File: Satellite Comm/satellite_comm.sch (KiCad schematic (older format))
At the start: 4 parts

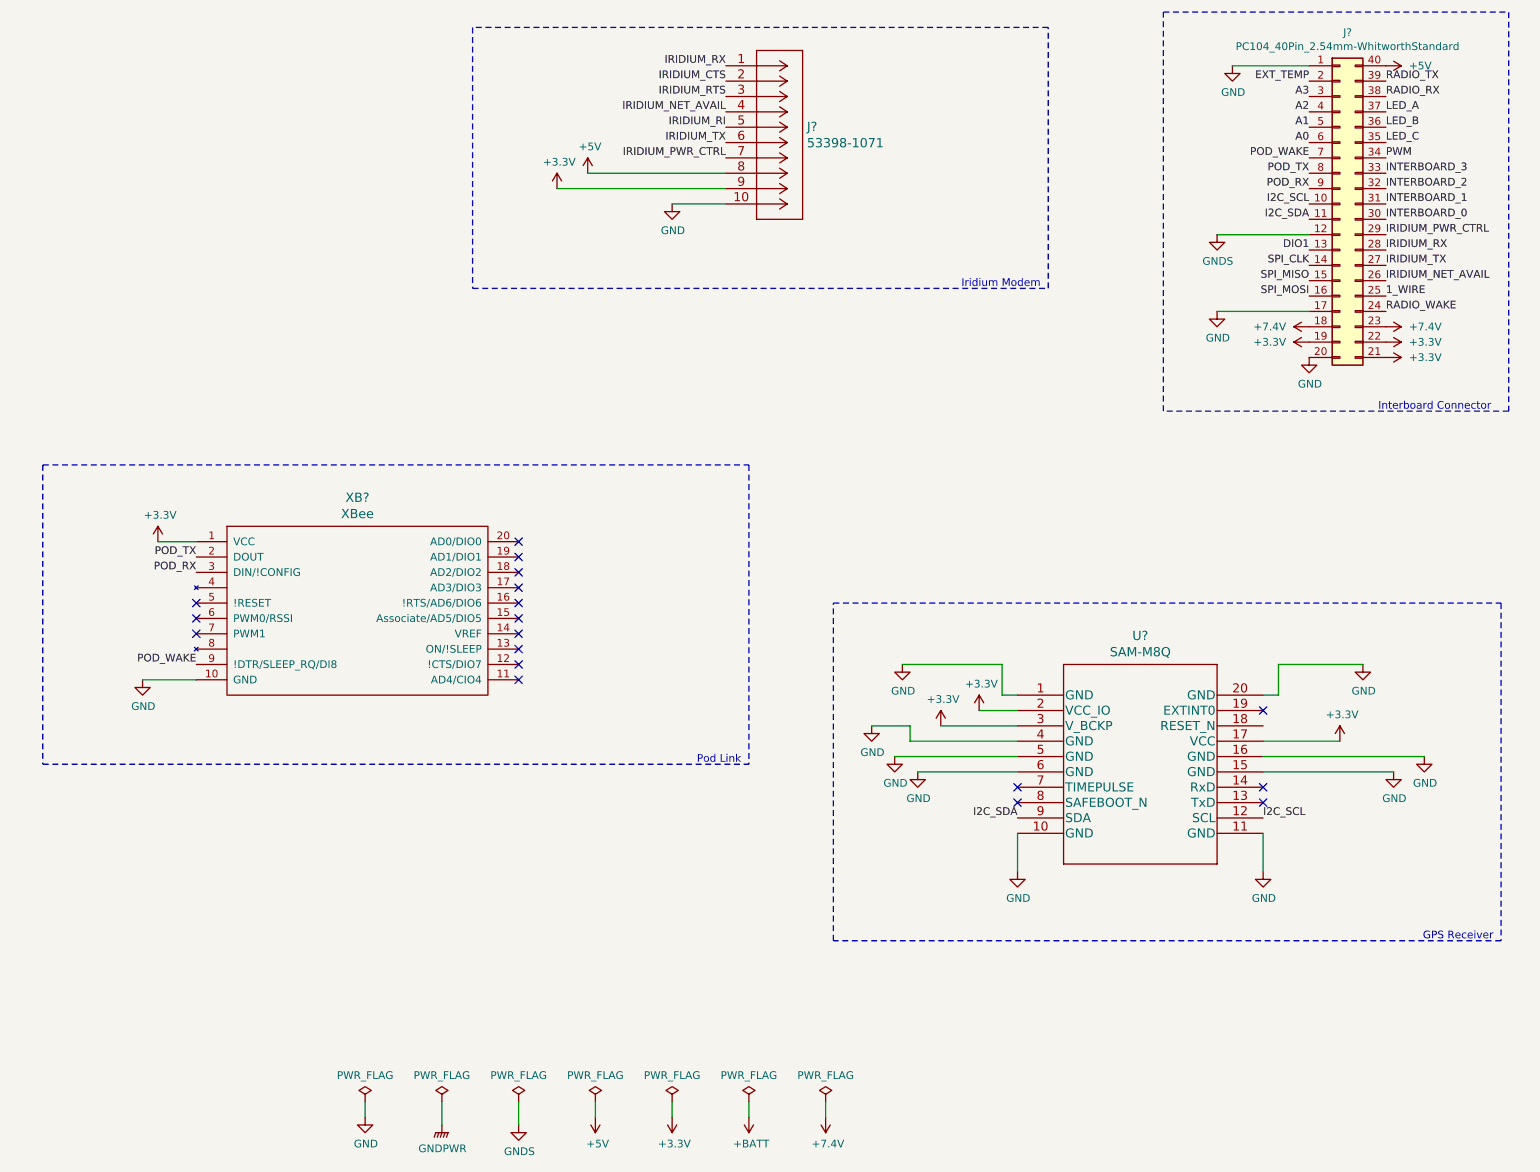
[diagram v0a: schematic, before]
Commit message: added the jumper/finished pin connections
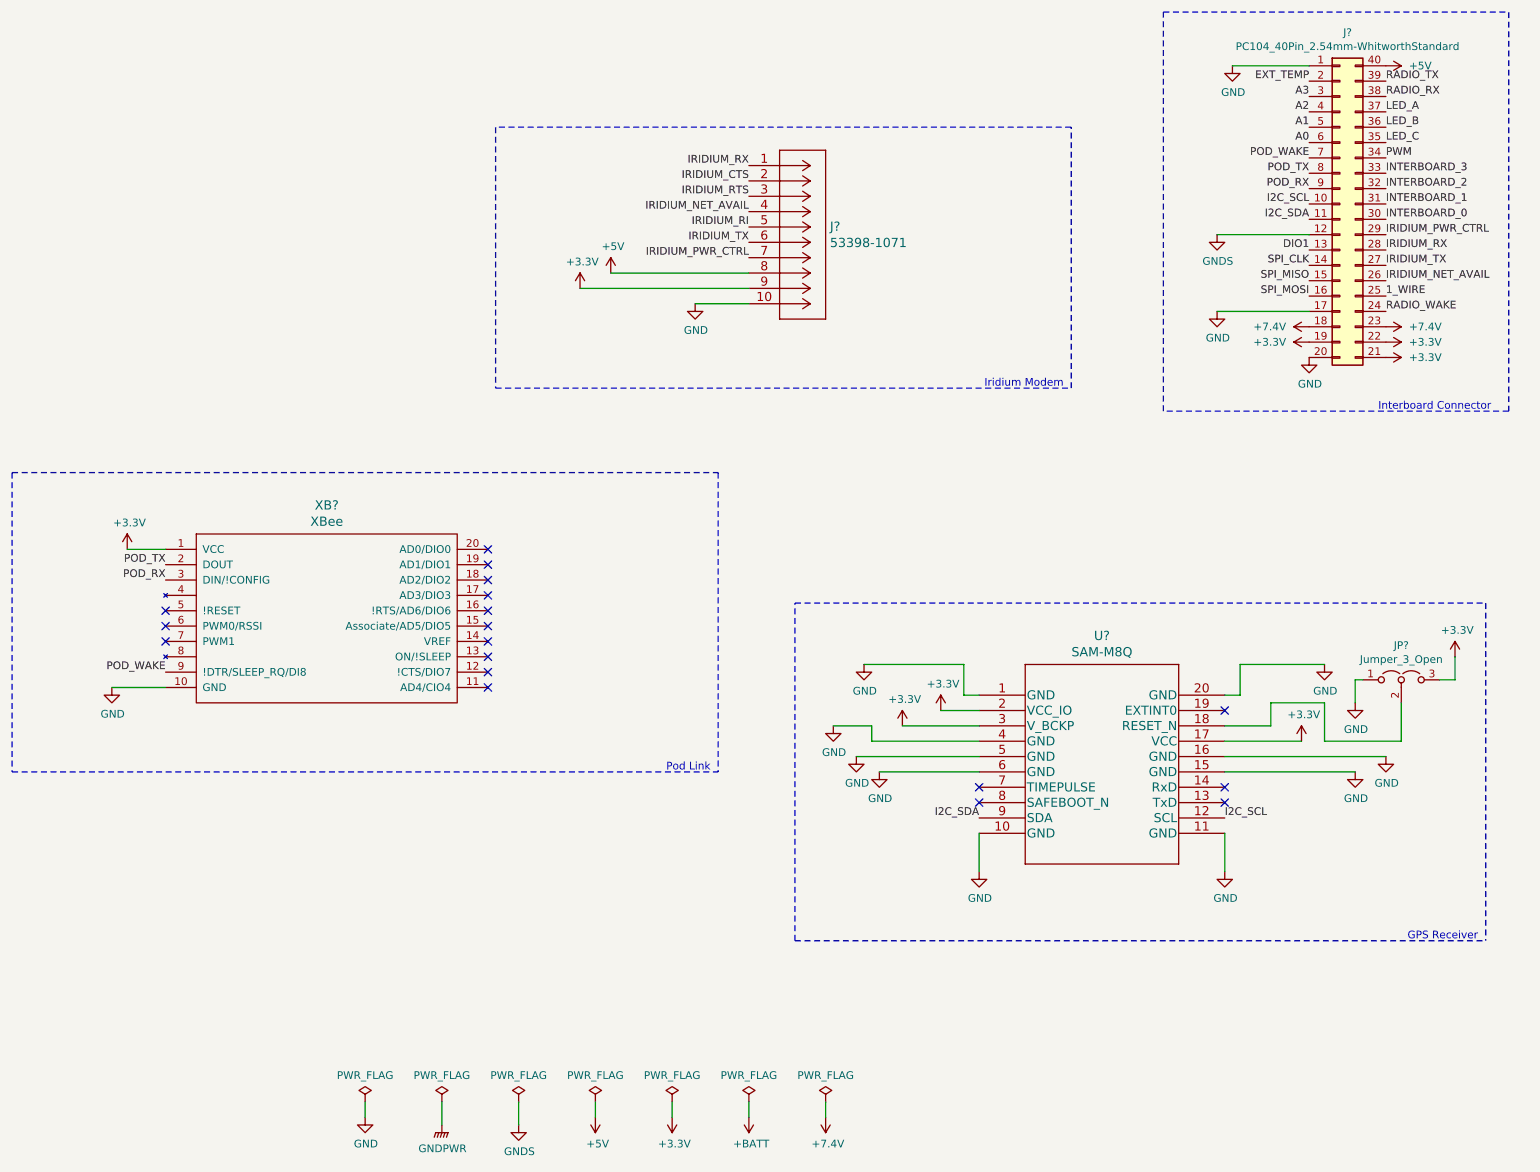
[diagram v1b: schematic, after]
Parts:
- added JP?: Jumper_3_Open, symbol Jumper:Jumper_3_Open
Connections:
- net +3V3: now also JP?.3 (B)
- net GND: now also JP?.1 (A)
- net at U?.18 (RESET_N): now also JP?.2 (C)
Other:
- moved on the sheet: J?, U?, XB?

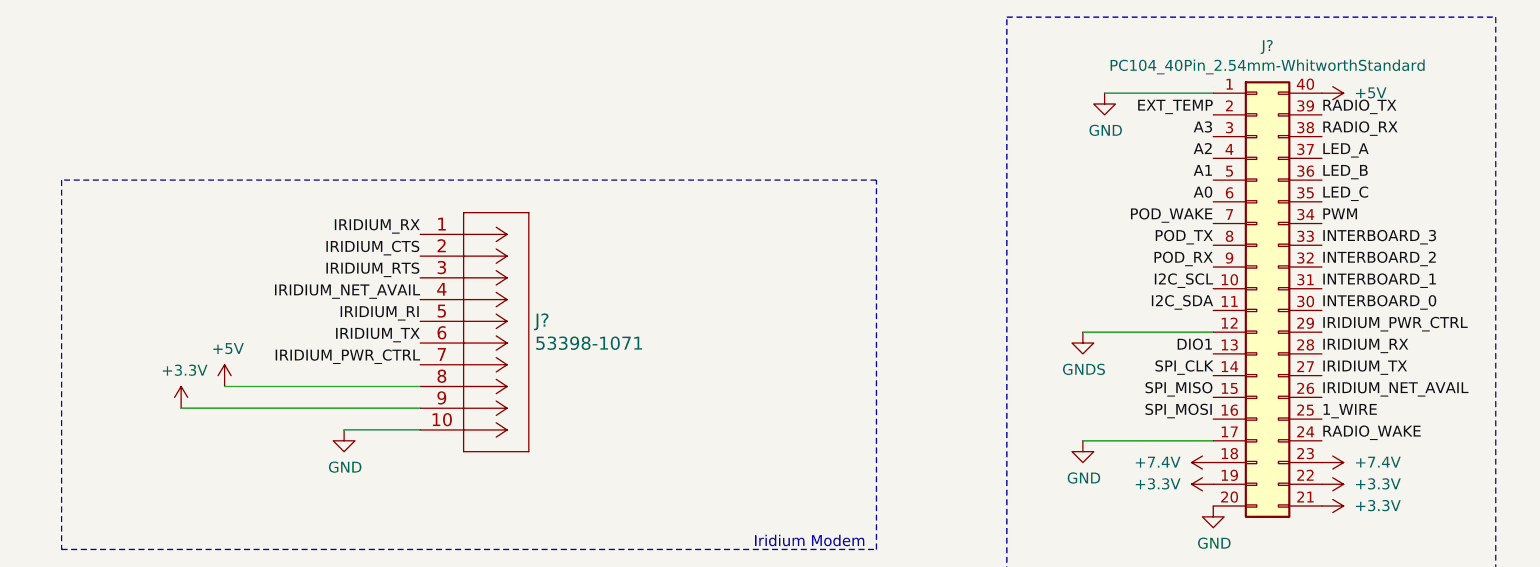
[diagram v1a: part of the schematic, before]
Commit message: corrected wrongly assigned pins
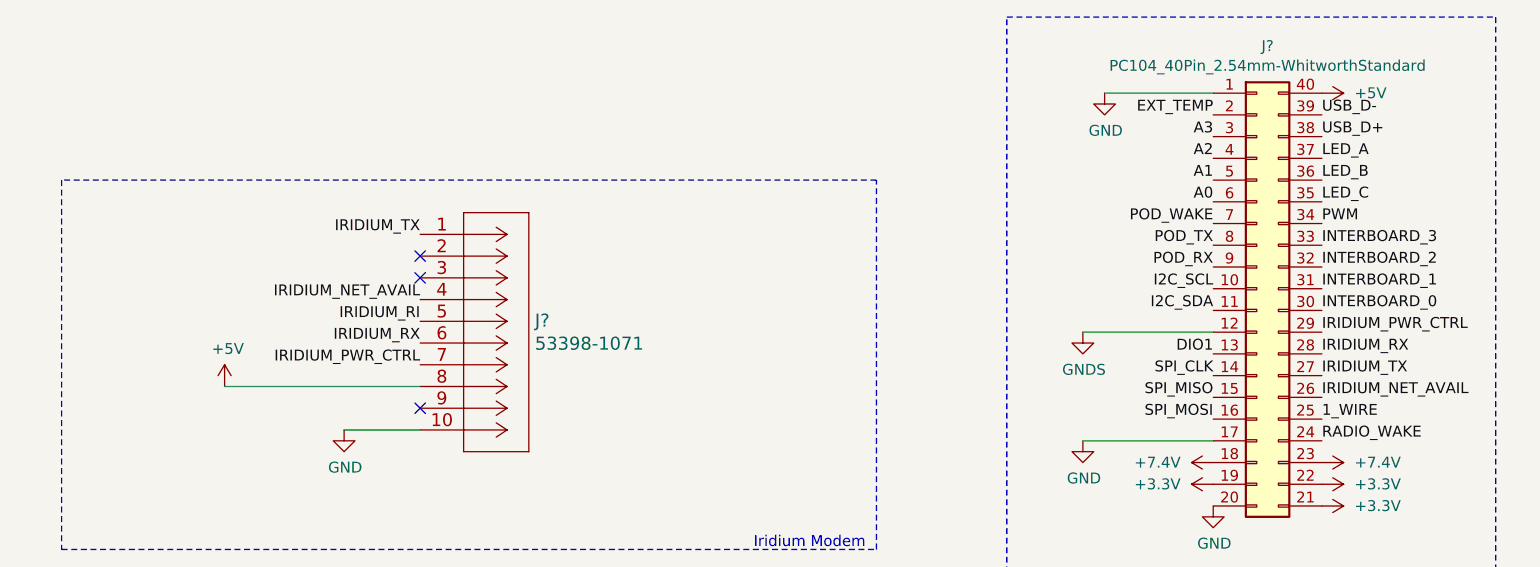
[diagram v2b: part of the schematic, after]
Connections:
- net +3V3: no longer J?.9
- net IRIDIUM_RX: now also J?.6; no longer J?.1
- net IRIDIUM_TX: now also J?.1; no longer J?.6
- net IRIDIUM_CTS: no longer names the net of J?.2
- net IRIDIUM_RTS: no longer names the net of J?.3
- net RADIO_RX renamed USB_D+
- net RADIO_TX renamed USB_D-
- no-connect marks 18 -> 21
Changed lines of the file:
@@
 $EndComp
 Text Label 9650 1000 0    50   ~ 0
-RADIO_TX
+USB_D-
 Text Label 9650 1100 0    50   ~ 0
-RADIO_RX
+USB_D+
 Text Label 9650 2500 0    50   ~ 0
 RADIO_WAKE
@@
 Wire Wire Line
 	5150 2450 5500 2450
-Text Label 5500 1550 2    50   ~ 0
+Text Label 5500 2050 2    50   ~ 0
 IRIDIUM_RX
 Text Label 5500 1850 2    50   ~ 0
 IRIDIUM_NET_AVAIL
-Text Label 5500 2050 2    50   ~ 0
+Text Label 5500 1550 2    50   ~ 0
 IRIDIUM_TX
 $Comp
@@
 	5500 2250 4600 2250
 $Comp
-L power:+3.3V #PWR?
-U 1 1 610C7ABA
-P 4400 2350
-F 0 "#PWR?" H 4400 2200 50  0001 C CNN
-F 1 "+3.3V" H 4415 2523 50  0000 C CNN
-F 2 "" H 4400 2350 50  0001 C CNN
-F 3 "" H 4400 2350 50  0001 C CNN
-	1    4400 2350
-	1    0    0    -1
-$EndComp
-Wire Wire Line
-	4400 2350 5500 2350
-$Comp
 L WhitworthStandard:XBee XB?
 U 1 1 610CDD59
@@
 	1    0    0    -1
 $EndComp
-Text Label 5500 1650 2    50   ~ 0
-IRIDIUM_CTS
-Text Label 5500 1750 2    50   ~ 0
-IRIDIUM_RTS
 Text Label 5500 1950 2    50   ~ 0
 IRIDIUM_RI
@@
 Wire Notes Line
 	5800 6600 10300 6600
+NoConn ~ 5500 2350
+NoConn ~ 5500 1650
+NoConn ~ 5500 1750
 $EndSCHEMATC
